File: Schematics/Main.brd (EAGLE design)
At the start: 100 x 80 mm, 12 parts, among them IC1 PIC12F1840, IC2 7805TV, Q1 BD139, X1 Fan, X2 Power

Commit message: All working now
Issues with repo resolved, back to normal!

Signed-off-by: Aljaž Srebrnič <a2piratesoft@gmail.com>
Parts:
- Q1: device transistor:TO126 -> transistor-power:TO126AV
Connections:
- net GND: now also Q1.E; no longer Q1.1
- net N$1: now also Q1.B; no longer Q1.3
- net N$7: now also Q1.C; no longer Q1.2
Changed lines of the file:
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@@
 <layers>
 <layer number="1" name="Top" color="4" fill="1" visible="yes" active="yes"/>
+<layer number="2" name="Route2" color="1" fill="3" visible="no" active="no"/>
+<layer number="3" name="Route3" color="4" fill="3" visible="no" active="no"/>
+<layer number="4" name="Route4" color="1" fill="4" visible="no" active="no"/>
+<layer number="5" name="Route5" color="4" fill="4" visible="no" active="no"/>
+<layer number="6" name="Route6" color="1" fill="8" visible="no" active="no"/>
+<layer number="7" name="Route7" color="4" fill="8" visible="no" active="no"/>
+<layer number="8" name="Route8" color="1" fill="2" visible="no" active="no"/>
+<layer number="9" name="Route9" color="4" fill="2" visible="no" active="no"/>
+<layer number="10" name="Route10" color="1" fill="7" visible="no" active="no"/>
+<layer number="11" name="Route11" color="4" fill="7" visible="no" active="no"/>
+<layer number="12" name="Route12" color="1" fill="5" visible="no" active="no"/>
+<layer number="13" name="Route13" color="4" fill="5" visible="no" active="no"/>
+<layer number="14" name="Route14" color="1" fill="6" visible="no" active="no"/>
+<layer number="15" name="Route15" color="4" fill="6" visible="no" active="no"/>
 <layer number="16" name="Bottom" color="1" fill="1" visible="yes" active="yes"/>
 <layer number="17" name="Pads" color="2" fill="1" visible="yes" active="yes"/>
@@
 </element>
 <element name="IC2" library="linear" package="TO220V" value="7805TV" x="66.04" y="72.39"/>
-<element name="Q1" library="transistor" package="TO126" value="BD139" x="46.99" y="62.23"/>
+<element name="Q1" library="transistor-power" package="TO126AV" value="BD139" x="46.99" y="62.23"/>
 <element name="S1" library="switch" package="5501" value="5501" x="82.55" y="68.58"/>
 <element name="S2" library="switch" package="5501" value="5501" x="82.55" y="53.34"/>
@@
 </signal>
 <signal name="N$7">
-<contactref element="Q1" pad="2"/>
+<contactref element="Q1" pad="C"/>
 <contactref element="X1" pad="1"/>
-<wire x1="46.99" y1="57.15" x2="53.34" y2="62.23" width="0" layer="19" extent="1-1"/>
+<wire x1="46.99" y1="60.96" x2="53.34" y2="62.23" width="0" layer="19" extent="1-1"/>
 </signal>
 <signal name="GND">
@@
 <contactref element="S2" pad="NO"/>
 <contactref element="S3" pad="NO"/>
-<contactref element="Q1" pad="1"/>
+<contactref element="Q1" pad="E"/>
 <contactref element="IR1" pad="GND"/>
 <contactref element="LED1" pad="K"/>
@@
 <wire x1="66.04" y1="69.85" x2="71.12" y2="57.15" width="0" layer="19" extent="1-1"/>
 <wire x1="53.34" y1="69.85" x2="66.04" y2="69.85" width="0" layer="19" extent="1-1"/>
-<wire x1="44.704" y1="57.15" x2="53.34" y2="69.85" width="0" layer="19" extent="1-1"/>
-<wire x1="48.26" y1="52.07" x2="44.704" y2="57.15" width="0" layer="19" extent="1-1"/>
+<wire x1="44.704" y1="60.96" x2="53.34" y2="69.85" width="0" layer="19" extent="1-1"/>
+<wire x1="48.26" y1="52.07" x2="44.704" y2="60.96" width="0" layer="19" extent="1-1"/>
 <wire x1="52.07" y1="44.45" x2="48.26" y2="52.07" width="0" layer="19" extent="1-1"/>
 </signal>
 <signal name="N$1">
-<contactref element="Q1" pad="3"/>
+<contactref element="Q1" pad="B"/>
 <contactref element="R2" pad="1"/>
-<wire x1="49.276" y1="57.15" x2="53.34" y2="54.61" width="0" layer="19" extent="1-1"/>
+<wire x1="49.276" y1="60.96" x2="53.34" y2="54.61" width="0" layer="19" extent="1-1"/>
 </signal>
 <signal name="N$6">

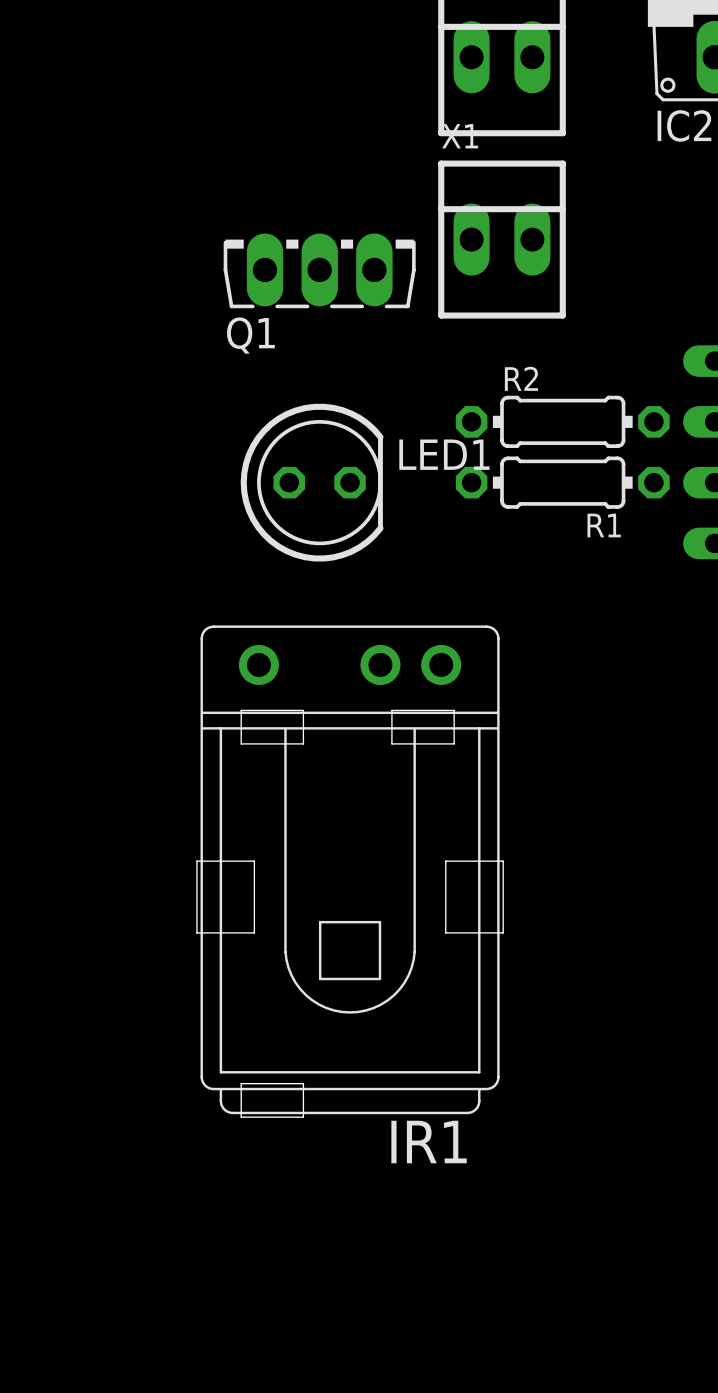
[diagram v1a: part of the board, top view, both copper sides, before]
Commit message: Ported schematics to next version of EAGLE
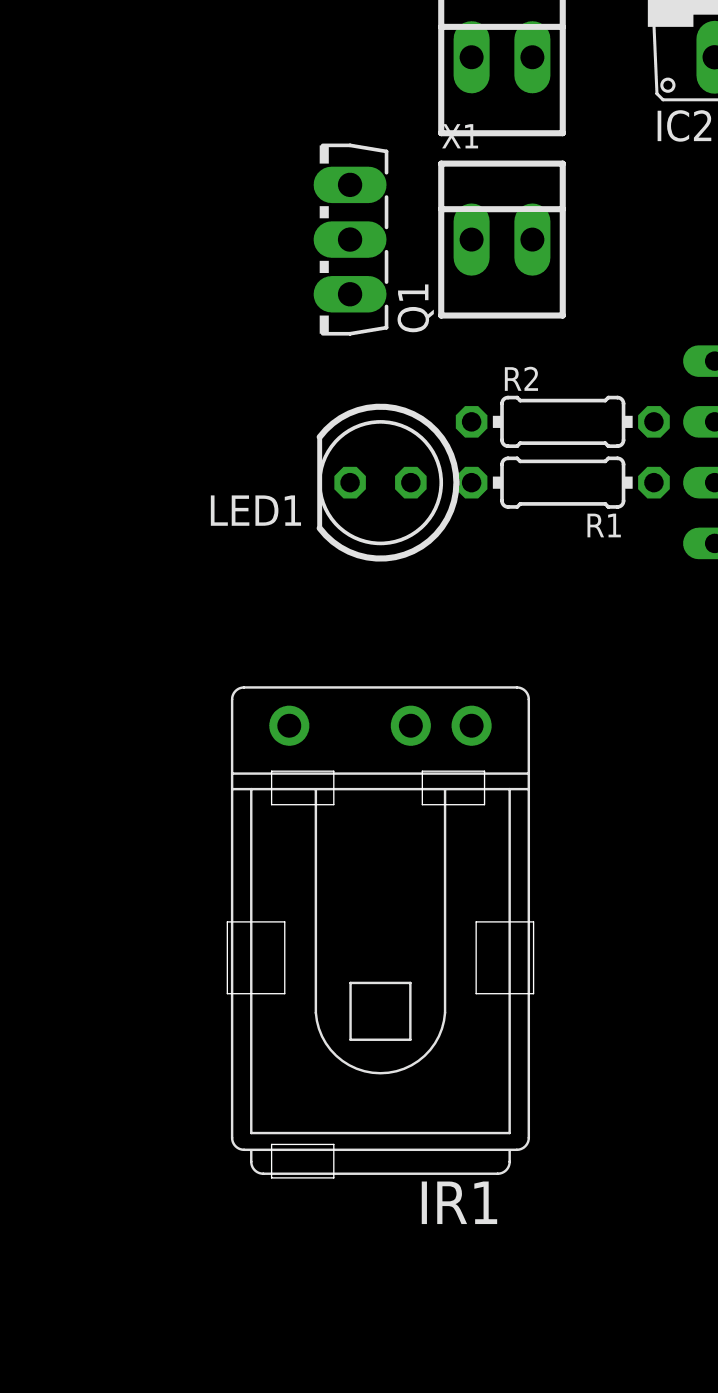
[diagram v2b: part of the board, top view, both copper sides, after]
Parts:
- moved IR1 2.84 mm to (49.5, 41.9)
- moved LED1 2.54 mm to (49.5, 52.1), turned to 180 degrees
- turned Q1 to 90 degrees
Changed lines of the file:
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@@
 </element>
 <element name="IC2" library="linear" package="TO220V" value="7805TV" x="66.04" y="72.39"/>
-<element name="Q1" library="transistor-power" package="TO126AV" value="BD139" x="46.99" y="62.23"/>
+<element name="Q1" library="transistor-power" package="TO126AV" value="BD139" x="46.99" y="62.23" rot="R90"/>
 <element name="S1" library="switch" package="5501" value="5501" x="82.55" y="68.58"/>
 <element name="S2" library="switch" package="5501" value="5501" x="82.55" y="53.34"/>
@@
 </element>
 <element name="R2" library="rcl" package="0204/7" value="2.2k" x="57.15" y="54.61"/>
-<element name="IR1" library="telefunken" package="TSOP17_TB1" value="TSOP1738TB1" x="48.26" y="44.45" rot="R90">
-<attribute name="MF" x="48.26" y="44.45" size="1.778" layer="27" rot="R90" display="off"/>
-<attribute name="MPN" x="48.26" y="44.45" size="1.778" layer="27" rot="R90" display="off"/>
-<attribute name="OC_FARNELL" value="unknown" x="48.26" y="44.45" size="1.778" layer="27" rot="R90" display="off"/>
-<attribute name="OC_NEWARK" value="unknown" x="48.26" y="44.45" size="1.778" layer="27" rot="R90" display="off"/>
+<element name="IR1" library="telefunken" package="TSOP17_TB1" value="TSOP1738TB1" x="49.53" y="41.91" rot="R90">
+<attribute name="MF" x="49.53" y="41.91" size="1.778" layer="27" rot="R90" display="off"/>
+<attribute name="MPN" x="49.53" y="41.91" size="1.778" layer="27" rot="R90" display="off"/>
+<attribute name="OC_FARNELL" value="unknown" x="49.53" y="41.91" size="1.778" layer="27" rot="R90" display="off"/>
+<attribute name="OC_NEWARK" value="unknown" x="49.53" y="41.91" size="1.778" layer="27" rot="R90" display="off"/>
 </element>
 <element name="R1" library="rcl" package="0204/7" value="" x="57.15" y="52.07" rot="R180"/>
-<element name="LED1" library="led" package="LED5MM" value="" x="46.99" y="52.07"/>
+<element name="LED1" library="led" package="LED5MM" value="" x="49.53" y="52.07" rot="R180"/>
 </elements>
 <signals>
@@
 <contactref element="Q1" pad="C"/>
 <contactref element="X1" pad="1"/>
-<wire x1="46.99" y1="60.96" x2="53.34" y2="62.23" width="0" layer="19" extent="1-1"/>
+<wire x1="48.26" y1="62.23" x2="53.34" y2="62.23" width="0" layer="19" extent="1-1"/>
 </signal>
 <signal name="GND">
@@
 <wire x1="66.04" y1="69.85" x2="71.12" y2="57.15" width="0" layer="19" extent="1-1"/>
 <wire x1="53.34" y1="69.85" x2="66.04" y2="69.85" width="0" layer="19" extent="1-1"/>
-<wire x1="44.704" y1="60.96" x2="53.34" y2="69.85" width="0" layer="19" extent="1-1"/>
-<wire x1="48.26" y1="52.07" x2="44.704" y2="60.96" width="0" layer="19" extent="1-1"/>
-<wire x1="52.07" y1="44.45" x2="48.26" y2="52.07" width="0" layer="19" extent="1-1"/>
+<wire x1="48.26" y1="59.944" x2="53.34" y2="69.85" width="0" layer="19" extent="1-1"/>
+<wire x1="48.26" y1="52.07" x2="48.26" y2="59.944" width="0" layer="19" extent="1-1"/>
+<wire x1="53.34" y1="41.91" x2="48.26" y2="52.07" width="0" layer="19" extent="1-1"/>
 </signal>
 <signal name="N$1">
 <contactref element="Q1" pad="B"/>
 <contactref element="R2" pad="1"/>
-<wire x1="49.276" y1="60.96" x2="53.34" y2="54.61" width="0" layer="19" extent="1-1"/>
+<wire x1="48.26" y1="64.516" x2="53.34" y2="54.61" width="0" layer="19" extent="1-1"/>
 </signal>
 <signal name="N$6">
@@
 <contactref element="IR1" pad="VS"/>
 <wire x1="63.5" y1="57.15" x2="68.58" y2="69.85" width="0" layer="19" extent="1-1"/>
-<wire x1="49.53" y1="44.45" x2="63.5" y2="57.15" width="0" layer="19" extent="1-1"/>
+<wire x1="50.8" y1="41.91" x2="63.5" y2="57.15" width="0" layer="19" extent="1-1"/>
 </signal>
 <signal name="N$2">
 <contactref element="IR1" pad="VO"/>
 <contactref element="IC1" pad="4"/>
-<wire x1="44.45" y1="44.45" x2="63.5" y2="49.53" width="0" layer="19" extent="1-1"/>
+<wire x1="45.72" y1="41.91" x2="63.5" y2="49.53" width="0" layer="19" extent="1-1"/>
 </signal>
 <signal name="N$8">
@@
 <contactref element="R1" pad="2"/>
 <contactref element="LED1" pad="A"/>
-<wire x1="45.72" y1="52.07" x2="53.34" y2="52.07" width="0" layer="19" extent="1-1"/>
+<wire x1="50.8" y1="52.07" x2="53.34" y2="52.07" width="0" layer="19" extent="1-1"/>
 </signal>
 </signals>
